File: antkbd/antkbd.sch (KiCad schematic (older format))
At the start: 16 parts

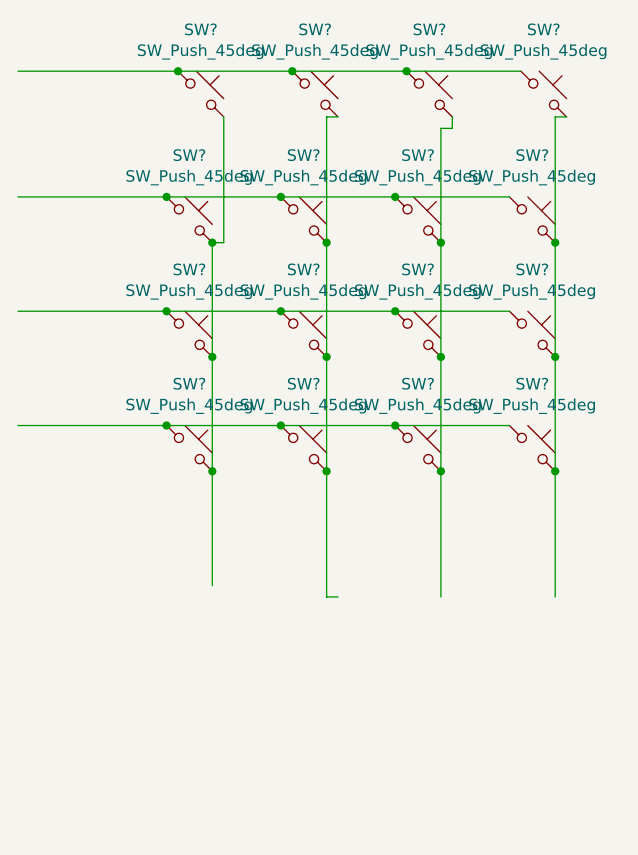
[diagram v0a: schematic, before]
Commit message: refactor controller
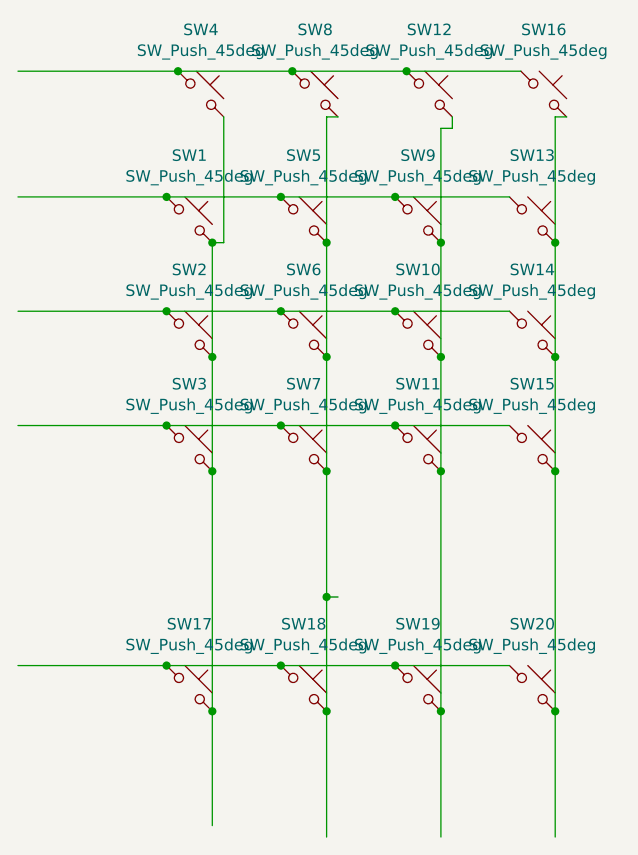
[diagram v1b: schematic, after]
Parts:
- added SW17, SW18, SW19, SW20: SW_Push_45deg, Button_Switch_THT:SW_PUSH_6mm, symbol Switch:SW_Push_45deg
- SW1, SW10, SW11, SW12, SW13, SW14, SW15, SW16, SW2, SW3, SW4, SW5, SW6, SW7, SW8, SW9: renamed from SW?; footprint (none) -> Button_Switch_THT:SW_PUSH_6mm
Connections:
- wire segments 38 -> 47
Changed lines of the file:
@@
 $EndDescr
 $Comp
-L Switch:SW_Push_45deg SW?
+L Switch:SW_Push_45deg SW4
 U 1 1 5DACD623
 P 2500 2500
-F 0 "SW?" H 2500 2781 50  0000 C CNN
+F 0 "SW4" H 2500 2781 50  0000 C CNN
 F 1 "SW_Push_45deg" H 2500 2690 50  0000 C CNN
-F 2 "" H 2500 2500 50  0001 C CNN
+F 2 "Button_Switch_THT:SW_PUSH_6mm" H 2500 2500 50  0001 C CNN
 F 3 "~" H 2500 2500 50  0001 C CNN
 	1    2500 2500
@@
 $EndComp
 $Comp
-L Switch:SW_Push_45deg SW?
+L Switch:SW_Push_45deg SW8
 U 1 1 5DACE325
 P 3000 2500
-F 0 "SW?" H 3000 2781 50  0000 C CNN
+F 0 "SW8" H 3000 2781 50  0000 C CNN
 F 1 "SW_Push_45deg" H 3000 2690 50  0000 C CNN
-F 2 "" H 3000 2500 50  0001 C CNN
+F 2 "Button_Switch_THT:SW_PUSH_6mm" H 3000 2500 50  0001 C CNN
 F 3 "~" H 3000 2500 50  0001 C CNN
 	1    3000 2500
@@
 $EndComp
 $Comp
-L Switch:SW_Push_45deg SW?
+L Switch:SW_Push_45deg SW12
 U 1 1 5DACE7AB
 P 3500 2500
-F 0 "SW?" H 3500 2781 50  0000 C CNN
+F 0 "SW12" H 3500 2781 50  0000 C CNN
 F 1 "SW_Push_45deg" H 3500 2690 50  0000 C CNN
-F 2 "" H 3500 2500 50  0001 C CNN
+F 2 "Button_Switch_THT:SW_PUSH_6mm" H 3500 2500 50  0001 C CNN
 F 3 "~" H 3500 2500 50  0001 C CNN
 	1    3500 2500
@@
 $EndComp
 $Comp
-L Switch:SW_Push_45deg SW?
+L Switch:SW_Push_45deg SW1
 U 1 1 5DACEC35
 P 2450 3050
-F 0 "SW?" H 2450 3331 50  0000 C CNN
+F 0 "SW1" H 2450 3331 50  0000 C CNN
 F 1 "SW_Push_45deg" H 2450 3240 50  0000 C CNN
-F 2 "" H 2450 3050 50  0001 C CNN
+F 2 "Button_Switch_THT:SW_PUSH_6mm" H 2450 3050 50  0001 C CNN
 F 3 "~" H 2450 3050 50  0001 C CNN
 	1    2450 3050
@@
 $EndComp
 $Comp
-L Switch:SW_Push_45deg SW?
+L Switch:SW_Push_45deg SW5
 U 1 1 5DACF537
 P 2950 3050
-F 0 "SW?" H 2950 3331 50  0000 C CNN
+F 0 "SW5" H 2950 3331 50  0000 C CNN
 F 1 "SW_Push_45deg" H 2950 3240 50  0000 C CNN
-F 2 "" H 2950 3050 50  0001 C CNN
+F 2 "Button_Switch_THT:SW_PUSH_6mm" H 2950 3050 50  0001 C CNN
 F 3 "~" H 2950 3050 50  0001 C CNN
 	1    2950 3050
@@
 $EndComp
 $Comp
-L Switch:SW_Push_45deg SW?
+L Switch:SW_Push_45deg SW9
 U 1 1 5DACF9B2
 P 3450 3050
-F 0 "SW?" H 3450 3331 50  0000 C CNN
+F 0 "SW9" H 3450 3331 50  0000 C CNN
 F 1 "SW_Push_45deg" H 3450 3240 50  0000 C CNN
-F 2 "" H 3450 3050 50  0001 C CNN
+F 2 "Button_Switch_THT:SW_PUSH_6mm" H 3450 3050 50  0001 C CNN
 F 3 "~" H 3450 3050 50  0001 C CNN
 	1    3450 3050
@@
 $EndComp
 $Comp
-L Switch:SW_Push_45deg SW?
+L Switch:SW_Push_45deg SW2
 U 1 1 5DACFD94
 P 2450 3550
-F 0 "SW?" H 2450 3831 50  0000 C CNN
+F 0 "SW2" H 2450 3831 50  0000 C CNN
 F 1 "SW_Push_45deg" H 2450 3740 50  0000 C CNN
-F 2 "" H 2450 3550 50  0001 C CNN
+F 2 "Button_Switch_THT:SW_PUSH_6mm" H 2450 3550 50  0001 C CNN
 F 3 "~" H 2450 3550 50  0001 C CNN
 	1    2450 3550
@@
 $EndComp
 $Comp
-L Switch:SW_Push_45deg SW?
+L Switch:SW_Push_45deg SW6
 U 1 1 5DAD06E0
 P 2950 3550
-F 0 "SW?" H 2950 3831 50  0000 C CNN
+F 0 "SW6" H 2950 3831 50  0000 C CNN
 F 1 "SW_Push_45deg" H 2950 3740 50  0000 C CNN
-F 2 "" H 2950 3550 50  0001 C CNN
+F 2 "Button_Switch_THT:SW_PUSH_6mm" H 2950 3550 50  0001 C CNN
 F 3 "~" H 2950 3550 50  0001 C CNN
 	1    2950 3550
@@
 $EndComp
 $Comp
-L Switch:SW_Push_45deg SW?
+L Switch:SW_Push_45deg SW10
 U 1 1 5DAD0B1E
 P 3450 3550
-F 0 "SW?" H 3450 3831 50  0000 C CNN
+F 0 "SW10" H 3450 3831 50  0000 C CNN
 F 1 "SW_Push_45deg" H 3450 3740 50  0000 C CNN
-F 2 "" H 3450 3550 50  0001 C CNN
+F 2 "Button_Switch_THT:SW_PUSH_6mm" H 3450 3550 50  0001 C CNN
 F 3 "~" H 3450 3550 50  0001 C CNN
 	1    3450 3550
@@
 $EndComp
 $Comp
-L Switch:SW_Push_45deg SW?
+L Switch:SW_Push_45deg SW3
 U 1 1 5DAD0F62
 P 2450 4050
-F 0 "SW?" H 2450 4331 50  0000 C CNN
+F 0 "SW3" H 2450 4331 50  0000 C CNN
 F 1 "SW_Push_45deg" H 2450 4240 50  0000 C CNN
-F 2 "" H 2450 4050 50  0001 C CNN
+F 2 "Button_Switch_THT:SW_PUSH_6mm" H 2450 4050 50  0001 C CNN
 F 3 "~" H 2450 4050 50  0001 C CNN
 	1    2450 4050
@@
 $EndComp
 $Comp
-L Switch:SW_Push_45deg SW?
+L Switch:SW_Push_45deg SW7
 U 1 1 5DAD14B4
 P 2950 4050
-F 0 "SW?" H 2950 4331 50  0000 C CNN
+F 0 "SW7" H 2950 4331 50  0000 C CNN
 F 1 "SW_Push_45deg" H 2950 4240 50  0000 C CNN
-F 2 "" H 2950 4050 50  0001 C CNN
+F 2 "Button_Switch_THT:SW_PUSH_6mm" H 2950 4050 50  0001 C CNN
 F 3 "~" H 2950 4050 50  0001 C CNN
 	1    2950 4050
@@
 $EndComp
 $Comp
-L Switch:SW_Push_45deg SW?
+L Switch:SW_Push_45deg SW11
 U 1 1 5DAD17F1
 P 3450 4050
-F 0 "SW?" H 3450 4331 50  0000 C CNN
+F 0 "SW11" H 3450 4331 50  0000 C CNN
 F 1 "SW_Push_45deg" H 3450 4240 50  0000 C CNN
-F 2 "" H 3450 4050 50  0001 C CNN
+F 2 "Button_Switch_THT:SW_PUSH_6mm" H 3450 4050 50  0001 C CNN
 F 3 "~" H 3450 4050 50  0001 C CNN
 	1    3450 4050
@@
 $EndComp
 $Comp
-L Switch:SW_Push_45deg SW?
+L Switch:SW_Push_45deg SW16
 U 1 1 5DAD32D9
 P 4000 2500
-F 0 "SW?" H 4000 2781 50  0000 C CNN
+F 0 "SW16" H 4000 2781 50  0000 C CNN
 F 1 "SW_Push_45deg" H 4000 2690 50  0000 C CNN
-F 2 "" H 4000 2500 50  0001 C CNN
+F 2 "Button_Switch_THT:SW_PUSH_6mm" H 4000 2500 50  0001 C CNN
 F 3 "~" H 4000 2500 50  0001 C CNN
 	1    4000 2500
@@
 $EndComp
 $Comp
-L Switch:SW_Push_45deg SW?
+L Switch:SW_Push_45deg SW13
 U 1 1 5DAD32E3
 P 3950 3050
-F 0 "SW?" H 3950 3331 50  0000 C CNN
+F 0 "SW13" H 3950 3331 50  0000 C CNN
 F 1 "SW_Push_45deg" H 3950 3240 50  0000 C CNN
-F 2 "" H 3950 3050 50  0001 C CNN
+F 2 "Button_Switch_THT:SW_PUSH_6mm" H 3950 3050 50  0001 C CNN
 F 3 "~" H 3950 3050 50  0001 C CNN
 	1    3950 3050
@@
 $EndComp
 $Comp
-L Switch:SW_Push_45deg SW?
+L Switch:SW_Push_45deg SW14
 U 1 1 5DAD32ED
 P 3950 3550
-F 0 "SW?" H 3950 3831 50  0000 C CNN
+F 0 "SW14" H 3950 3831 50  0000 C CNN
 F 1 "SW_Push_45deg" H 3950 3740 50  0000 C CNN
-F 2 "" H 3950 3550 50  0001 C CNN
+F 2 "Button_Switch_THT:SW_PUSH_6mm" H 3950 3550 50  0001 C CNN
 F 3 "~" H 3950 3550 50  0001 C CNN
 	1    3950 3550
@@
 $EndComp
 $Comp
-L Switch:SW_Push_45deg SW?
+L Switch:SW_Push_45deg SW15
 U 1 1 5DAD32F7
 P 3950 4050
-F 0 "SW?" H 3950 4331 50  0000 C CNN
+F 0 "SW15" H 3950 4331 50  0000 C CNN
 F 1 "SW_Push_45deg" H 3950 4240 50  0000 C CNN
-F 2 "" H 3950 4050 50  0001 C CNN
+F 2 "Button_Switch_THT:SW_PUSH_6mm" H 3950 4050 50  0001 C CNN
 F 3 "~" H 3950 4050 50  0001 C CNN
 	1    3950 4050
@@
 Connection ~ 2550 4150
 Wire Wire Line
-	2550 4150 2550 4650
-Wire Wire Line
 	3100 2600 3050 2600
 Wire Wire Line
@@
 Connection ~ 3550 4150
 Wire Wire Line
-	3550 4150 3550 4700
-Wire Wire Line
 	4100 2600 4050 2600
 Wire Wire Line
@@
 	4050 3650 4050 4150
 Connection ~ 4050 4150
-Wire Wire Line
-	4050 4150 4050 4700
+$Comp
+L Switch:SW_Push_45deg SW17
+U 1 1 5DAE1A29
+P 2450 5100
+F 0 "SW17" H 2450 5381 50  0000 C CNN
+F 1 "SW_Push_45deg" H 2450 5290 50  0000 C CNN
+F 2 "Button_Switch_THT:SW_PUSH_6mm" H 2450 5100 50  0001 C CNN
+F 3 "~" H 2450 5100 50  0001 C CNN
+	1    2450 5100
+	1    0    0    -1
+$EndComp
+$Comp
+L Switch:SW_Push_45deg SW18
+U 1 1 5DAE1A33
+P 2950 5100
+F 0 "SW18" H 2950 5381 50  0000 C CNN
+F 1 "SW_Push_45deg" H 2950 5290 50  0000 C CNN
+F 2 "Button_Switch_THT:SW_PUSH_6mm" H 2950 5100 50  0001 C CNN
+F 3 "~" H 2950 5100 50  0001 C CNN
+	1    2950 5100
+	1    0    0    -1
+$EndComp
+$Comp
+L Switch:SW_Push_45deg SW19
+U 1 1 5DAE1A3D
+P 3450 5100
+F 0 "SW19" H 3450 5381 50  0000 C CNN
+F 1 "SW_Push_45deg" H 3450 5290 50  0000 C CNN
+F 2 "Button_Switch_THT:SW_PUSH_6mm" H 3450 5100 50  0001 C CNN
+F 3 "~" H 3450 5100 50  0001 C CNN
+	1    3450 5100
+	1    0    0    -1
+$EndComp
+$Comp
+L Switch:SW_Push_45deg SW20
+U 1 1 5DAE1A47
+P 3950 5100
+F 0 "SW20" H 3950 5381 50  0000 C CNN
+F 1 "SW_Push_45deg" H 3950 5290 50  0000 C CNN
+F 2 "Button_Switch_THT:SW_PUSH_6mm" H 3950 5100 50  0001 C CNN
+F 3 "~" H 3950 5100 50  0001 C CNN
+	1    3950 5100
+	1    0    0    -1
+$EndComp
+Wire Wire Line
+	3850 5000 3350 5000
+Connection ~ 2350 5000
+Wire Wire Line
+	2350 5000 1700 5000
+Connection ~ 2850 5000
+Wire Wire Line
+	2850 5000 2350 5000
+Connection ~ 3350 5000
+Wire Wire Line
+	3350 5000 2850 5000
+Connection ~ 2550 5200
+Wire Wire Line
+	2550 5200 2550 5700
+Wire Wire Line
+	3050 4700 3050 5200
+Connection ~ 3050 5200
+Wire Wire Line
+	3050 5200 3050 5750
+Connection ~ 3550 5200
+Wire Wire Line
+	3550 5200 3550 5750
+Connection ~ 4050 5200
+Wire Wire Line
+	4050 5200 4050 5750
+Connection ~ 3050 4700
+Wire Wire Line
+	3550 4150 3550 5200
+Wire Wire Line
+	4050 4150 4050 5200
+Wire Wire Line
+	2550 4150 2550 5200
 $EndSCHEMATC
